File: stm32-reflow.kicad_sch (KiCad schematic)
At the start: 0 parts

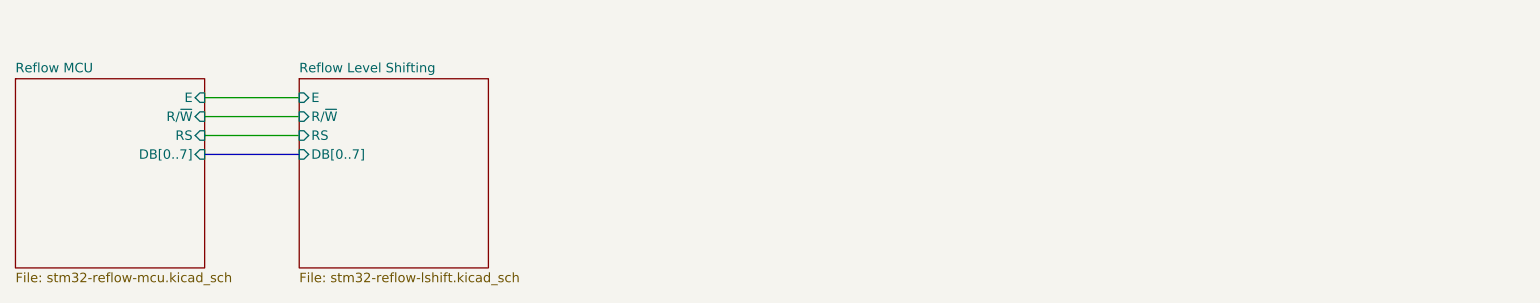
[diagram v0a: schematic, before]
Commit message: initial routing, added power supply source
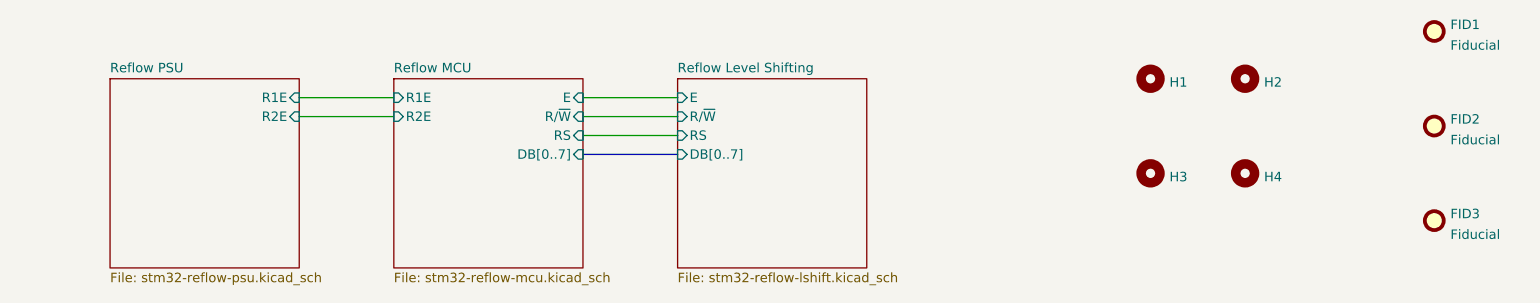
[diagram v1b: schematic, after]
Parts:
- added FID1, FID2, FID3: Fiducial, Fiducial:Fiducial_0.75mm_Mask2.25mm, symbol Mechanical:Fiducial
- added H1, H2, H3, H4: MountingHole, MountingHole:MountingHole_2.7mm_M2.5_Pad_Via, symbol Mechanical:MountingHole
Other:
- added sheet Reflow PSU (stm32-reflow-psu.kicad_sch)
- sheet Reflow MCU ports: added R1E, R2E; removed none

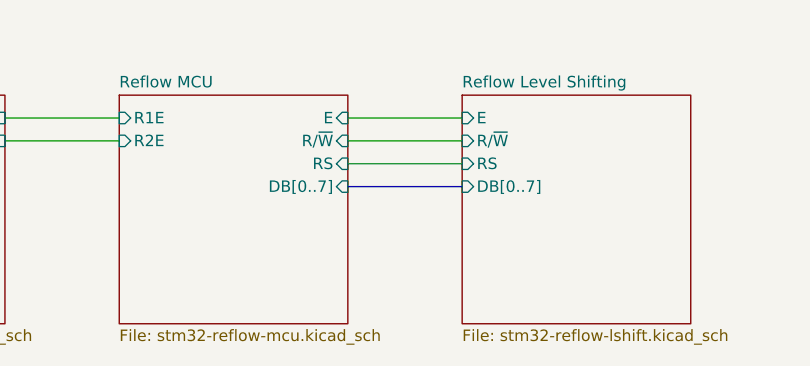
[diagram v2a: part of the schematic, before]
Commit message: downsized resistor network to 10
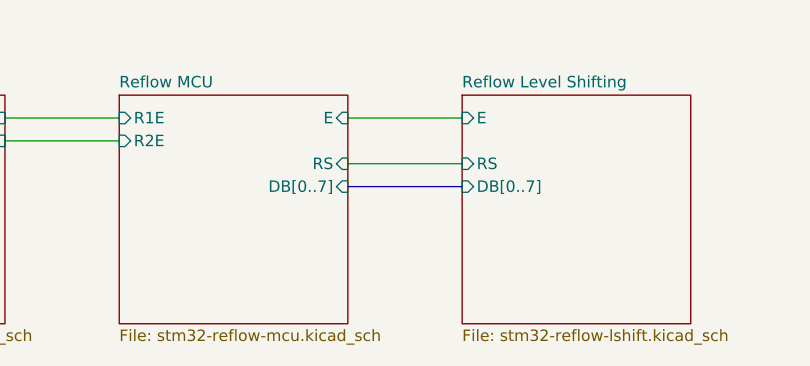
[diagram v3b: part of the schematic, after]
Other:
- sheet Reflow Level Shifting ports: added none; removed R/~{W}
- sheet Reflow MCU ports: added none; removed R/~{W}
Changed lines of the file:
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@@
-    (stroke (width 0) (type default) (color 0 0 0 0))
-  )
-  (wire (pts (xy 139.7 68.58) (xy 152.4 68.58))
     (stroke (width 0) (type default) (color 0 0 0 0))
   )
@@
       (effects (font (size 1.27 1.27)) (justify left))
     )
-    (pin "R{slash}~{W}" input (at 152.4 68.58 180)
-      (effects (font (size 1.27 1.27)) (justify left))
-    )
     (pin "RS" input (at 152.4 71.12 180)
       (effects (font (size 1.27 1.27)) (justify left))
@@
       (effects (font (size 1.27 1.27)) (justify right))
     )
-    (pin "R{slash}~{W}" input (at 139.7 68.58 0)
-      (effects (font (size 1.27 1.27)) (justify right))
-    )
     (pin "RS" input (at 139.7 71.12 0)
       (effects (font (size 1.27 1.27)) (justify right))
@@
       (reference "Q1") (unit 1) (value "2N7002") (footprint "Package_TO_SOT_SMD:SOT-23")
     )
-    (path "/bd08278b-4287-4daa-92d4-6c7e541ec8a9/7109660b-bf89-4b81-bf9b-bb7cc1066e21"
-      (reference "Q2") (unit 1) (value "2N7002") (footprint "Package_TO_SOT_SMD:SOT-23")
-    )
     (path "/bd08278b-4287-4daa-92d4-6c7e541ec8a9/29f28fdb-bbef-4971-98bd-9d4774417fc2"
       (reference "Q3") (unit 1) (value "2N7002") (footprint "Package_TO_SOT_SMD:SOT-23")
@@
       (reference "R5") (unit 1) (value "10k") (footprint "Resistor_SMD:R_0603_1608Metric")
     )
-    (path "/bd08278b-4287-4daa-92d4-6c7e541ec8a9/a20bfea7-348f-4161-9d7c-d6ccc42890df"
-      (reference "RN1") (unit 1) (value "10k") (footprint "Resistor_THT:R_Array_SIP12")
-    )
-    (path "/bd08278b-4287-4daa-92d4-6c7e541ec8a9/1319110e-3cc5-415e-88ce-8fdb7e9cfb40"
-      (reference "RN2") (unit 1) (value "10k") (footprint "Resistor_THT:R_Array_SIP12")
+    (path "/bd08278b-4287-4daa-92d4-6c7e541ec8a9/e80531bc-e2e7-4719-b9a4-2382e64235f3"
+      (reference "RN1") (unit 1) (value "10k") (footprint "Resistor_THT:R_Array_SIP11")
+    )
+    (path "/bd08278b-4287-4daa-92d4-6c7e541ec8a9/d1703d80-0d79-4d43-9e52-a4ec2afb81b2"
+      (reference "RN2") (unit 1) (value "10k") (footprint "Resistor_THT:R_Array_SIP11")
     )
     (path "/bd08278b-4287-4daa-92d4-6c7e541ec8a9/b8b1f6f8-bfc5-4cce-b4a8-26a1a9c0853f"

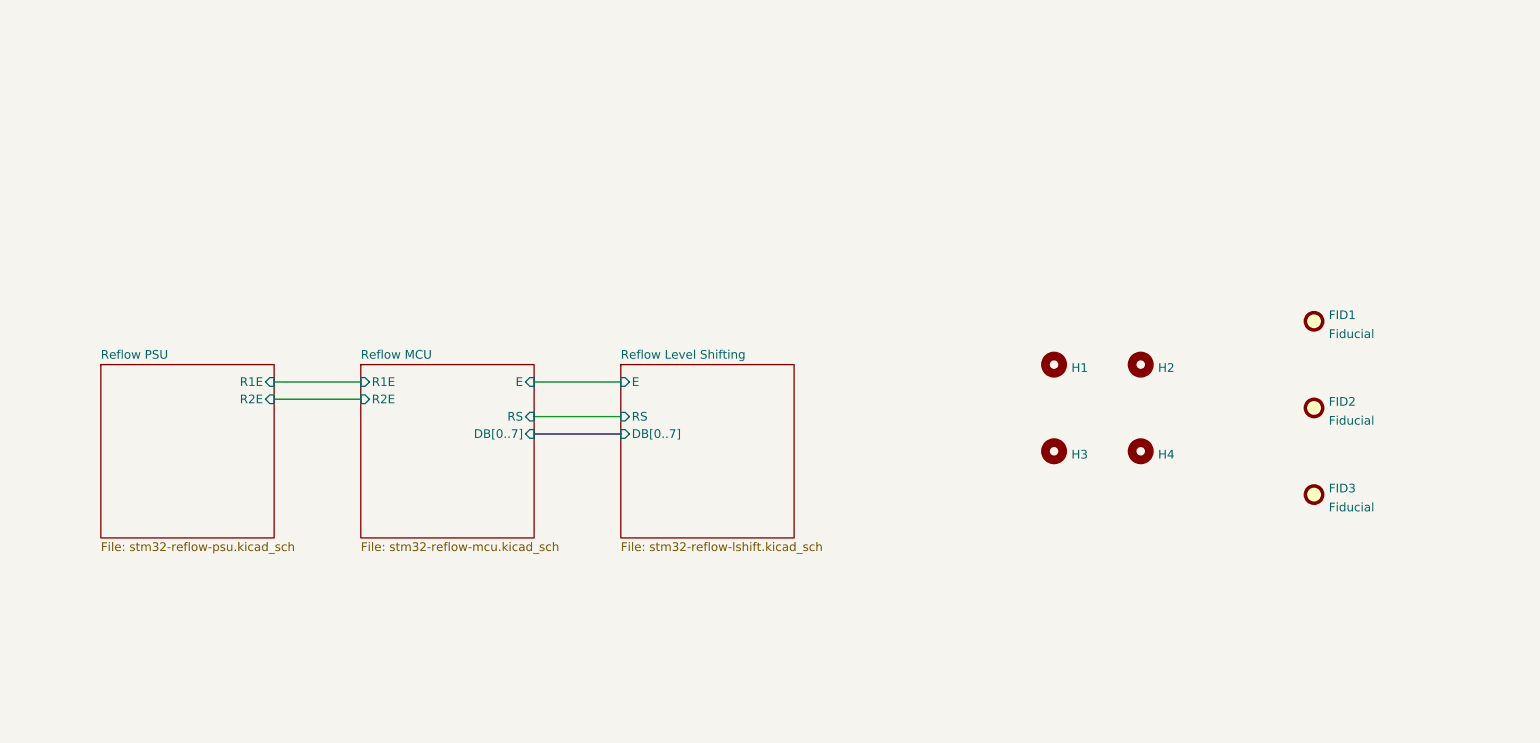
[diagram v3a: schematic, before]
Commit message: consolidated schematics for clarity, labeling and organization
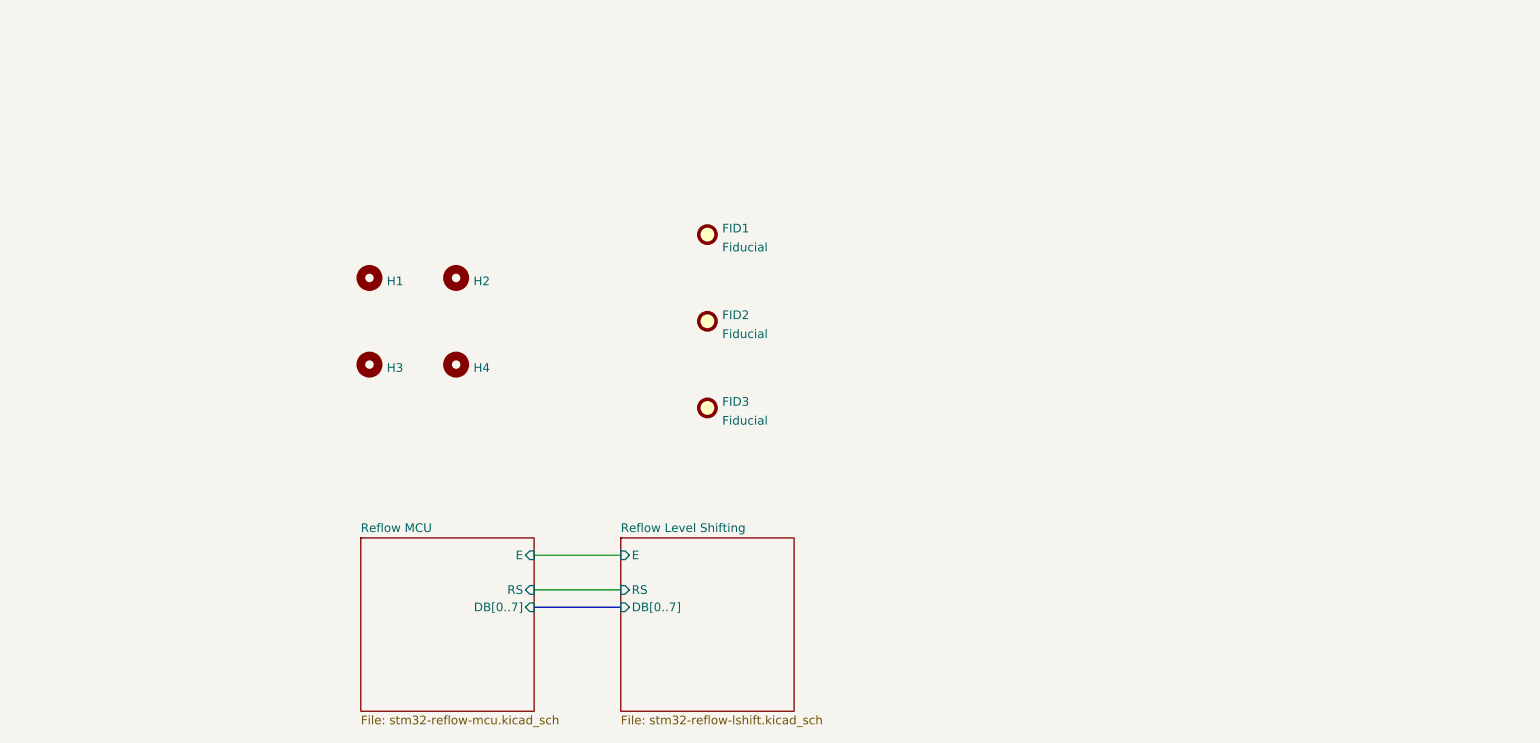
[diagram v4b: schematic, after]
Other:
- removed sheet Reflow PSU
- sheet Reflow MCU ports: added none; removed R1E, R2E
- company: (none) -> de Byl Technologies, LLC
- title: (none) -> STM32 Reflow Controller
- moved on the sheet: FID1, FID2, FID3, H1, H2, H3, H4
